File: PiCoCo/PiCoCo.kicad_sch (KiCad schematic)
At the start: 42 parts, among them P1 COCO-CART, Q2 2N7002, U1 Pico 2, U10 SN74LVC8T245DW, U11 SN74LVC245AD, U12 SN74LVC245AD, U13 SN74LVC245AD, U14 AMS1117-3.3, U15 SN74LVC1G11

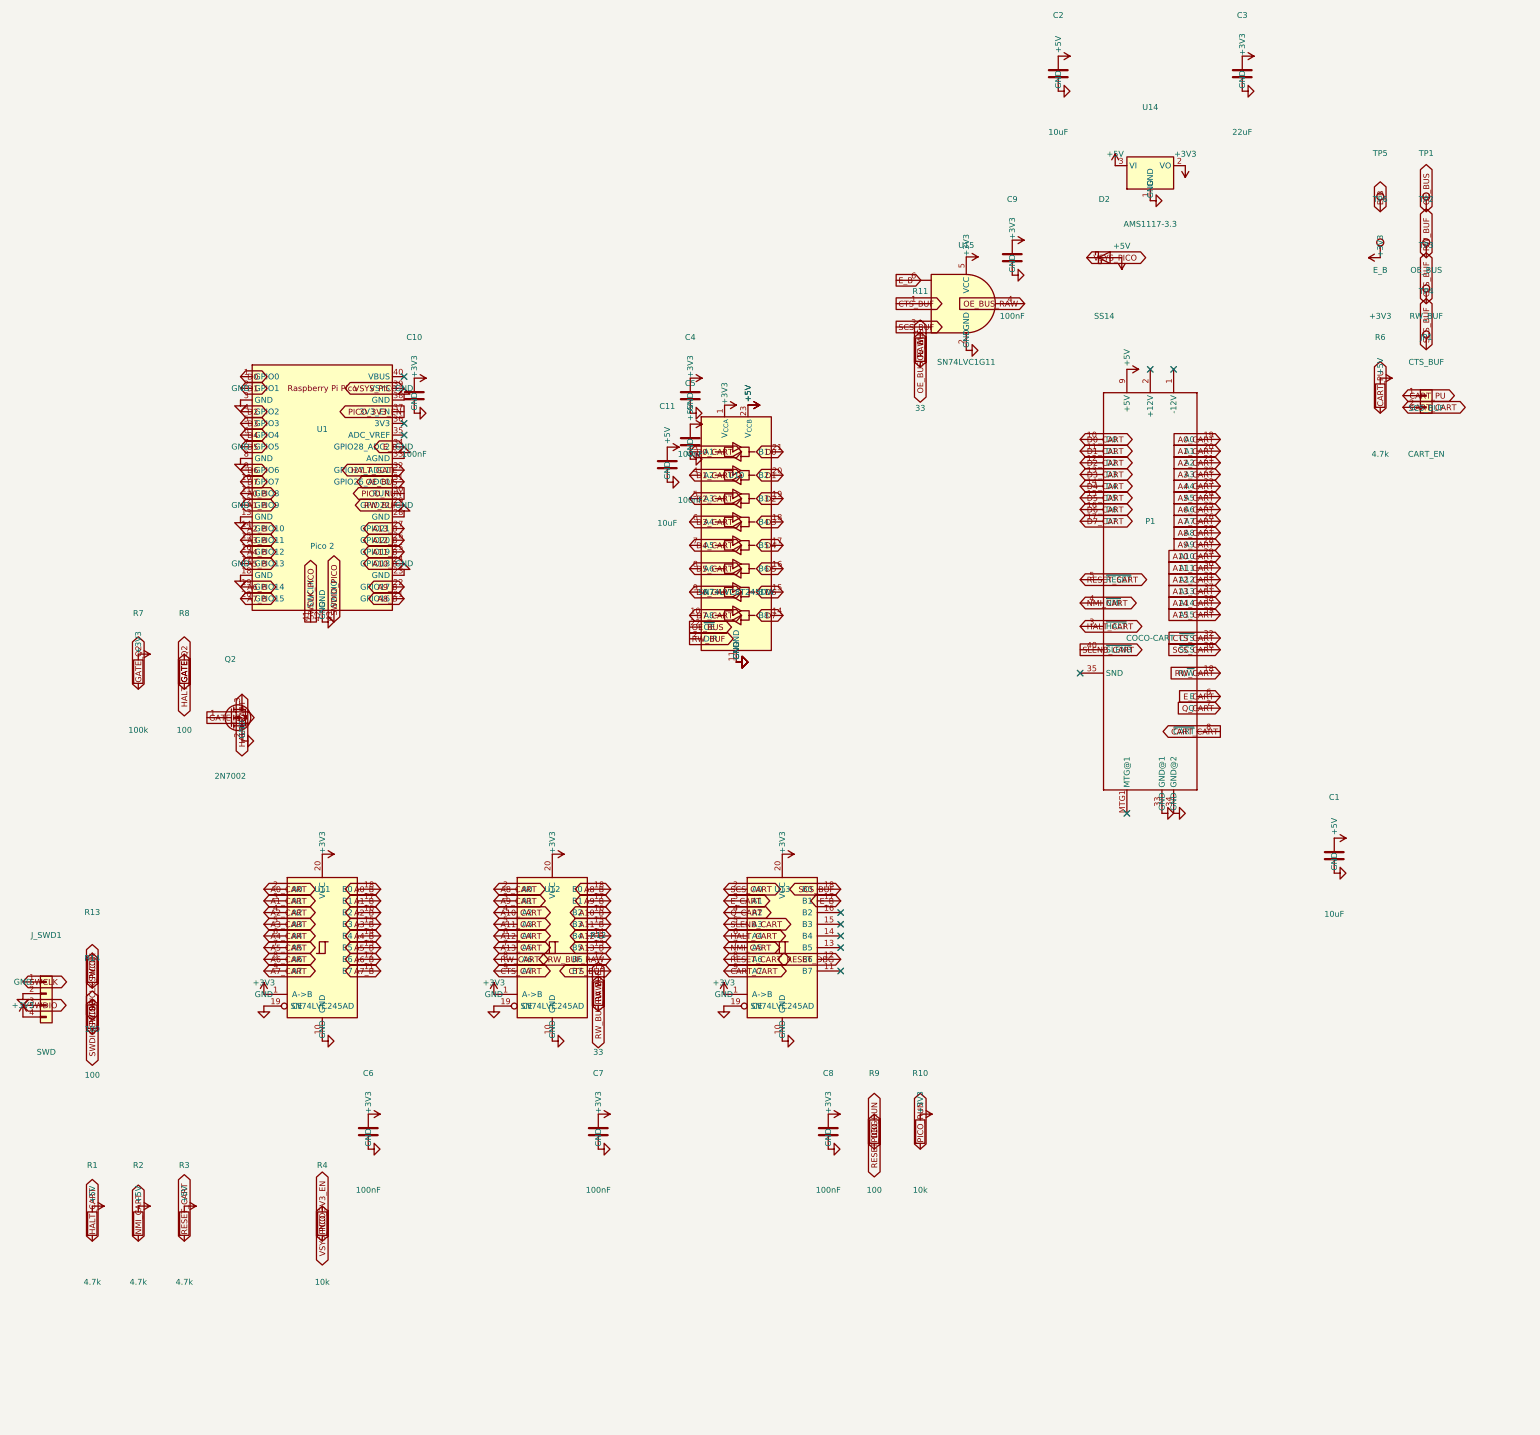
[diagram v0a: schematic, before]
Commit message: kicad: schematic v2.3 (LVC245 data buffer, 74LVC00 NAND-NAND decode, Plus-W pads, JP2/JP3, sound stage, LCSC properties, self-check)
Co-Authored-By: Claude Sonnet 5 <noreply@anthropic.com>
Claude-Session: https://claude.ai/code/session_013jbrP69zFzwzxjawTKy2c7
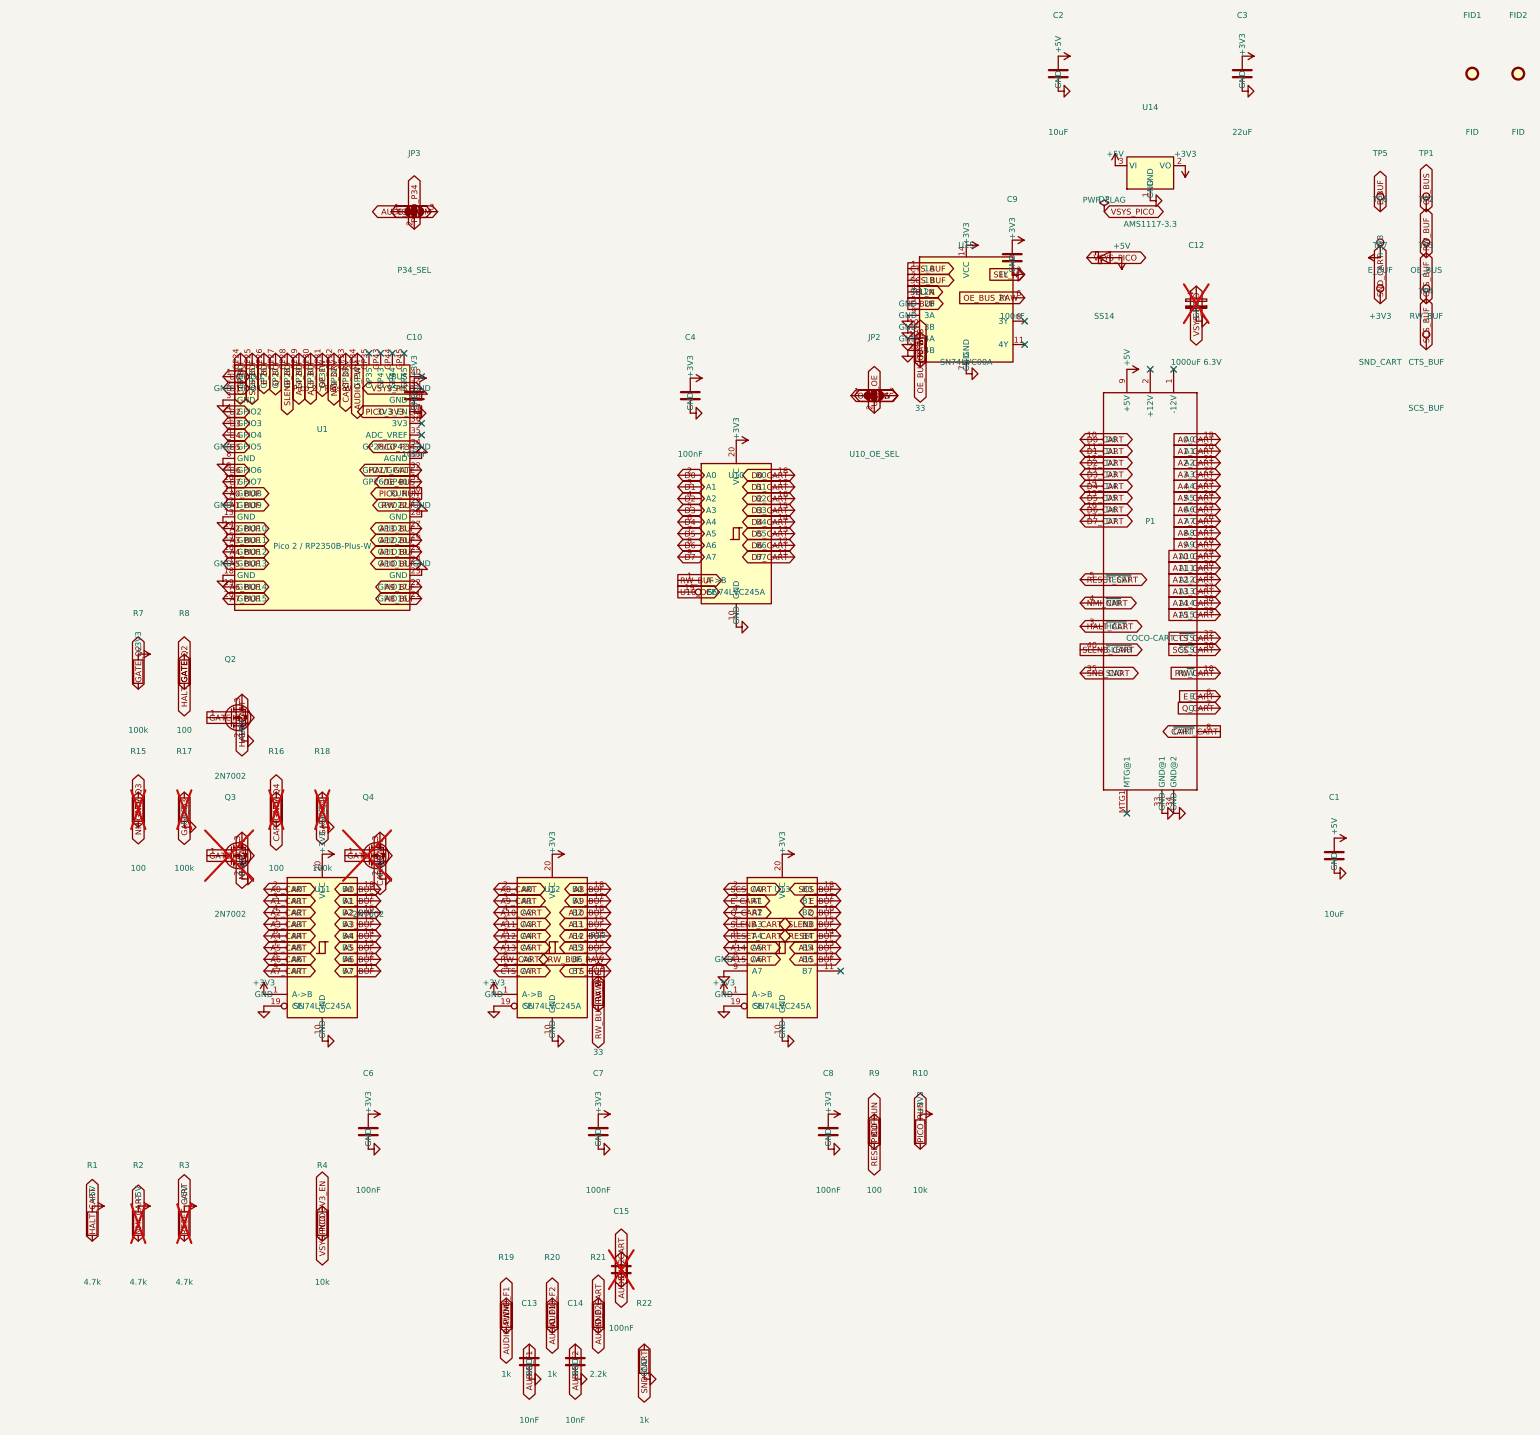
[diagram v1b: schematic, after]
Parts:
- removed C11: 10uF, Capacitor_SMD:C_0805_2012Metric, symbol Device:C
- removed C5: 100nF, Capacitor_SMD:C_0805_2012Metric, symbol Device:C
- removed JP1: CART_EN, Connector_PinHeader_2.54mm:PinHeader_1x02_P2.54mm_Vertical, symbol Connector_Generic:Conn_01x02
- removed J_SWD1: SWD, Connector_PinHeader_2.54mm:PinHeader_1x04_P2.54mm_Vertical, symbol Connector_Generic:Conn_01x04
- removed R13, R14: 100, Resistor_SMD:R_0805_2012Metric, symbol Device:R
- removed R6: 4.7k, Resistor_SMD:R_0805_2012Metric, symbol Device:R
- removed U1: Pico 2, PiCoCo:RPi_Pico_SMD_TH, symbol PiCoCo:Pico
- removed U10: SN74LVC8T245DW, Package_SO:SOIC-24W_7.5x15.4mm_P1.27mm, symbol Logic_LevelTranslator:SN74LVC8T245
- removed U15: SN74LVC1G11, Package_TO_SOT_SMD:SOT-363_SC-70-6, symbol 74xGxx:74LVC1G11
- added C12: 1000uF 6.3V, Capacitor_SMD:CP_Elec_8x10, symbol Device:C_Polarized
- added C13, C14: 10nF, Capacitor_SMD:C_0805_2012Metric, symbol Device:C
- added C15: 100nF, Capacitor_SMD:C_0805_2012Metric, symbol Device:C
- added FID1, FID2: FID, Fiducial:Fiducial_1mm_Mask2mm, symbol Mechanical:Fiducial
- added JP2: U10_OE_SEL, Jumper:SolderJumper-3_P1.3mm_Bridged12_RoundedPad1.0x1.5mm, symbol Jumper:SolderJumper_3_Bridged12
- added JP3: P34_SEL, Jumper:SolderJumper-3_P1.3mm_Bridged12_RoundedPad1.0x1.5mm, symbol Jumper:SolderJumper_3_Bridged12
- added Q3, Q4: 2N7002, Package_TO_SOT_SMD:SOT-23, symbol Transistor_FET:Q_NMOS_GSD
- added R15, R16: 100, Resistor_SMD:R_0805_2012Metric, symbol Device:R
- added R17, R18: 100k, Resistor_SMD:R_0805_2012Metric, symbol Device:R
- added R19, R20, R22: 1k, Resistor_SMD:R_0805_2012Metric, symbol Device:R
- added R21: 2.2k, Resistor_SMD:R_0805_2012Metric, symbol Device:R
- added TP7: SND_CART, TestPoint:TestPoint_Pad_1.0x1.0mm, symbol Connector:TestPoint
- added U1: Pico 2 / RP2350B-Plus-W, PiCoCo:Pico-Carrier, symbol PiCoCo:Pico-Carrier
- added U10: SN74LVC245A, Package_SO:SOIC-20W_7.5x12.8mm_P1.27mm, symbol 74xx:74LS245
- added U15: SN74LVC00A, Package_SO:SOIC-14_3.9x8.7mm_P1.27mm, symbol PiCoCo:74LVC00
- C1, C2: LCSC (none) -> C15850; MPN (none) -> 0805 10uF
- C10, C4, C6, C7, C8, C9: LCSC (none) -> C49678; MPN (none) -> 0805 100nF
- C3: LCSC (none) -> C45783; MPN (none) -> 0805 22uF
- D2: LCSC (none) -> C2480; MPN (none) -> SS14
- P1, TP1, TP2, TP3, TP4, TP6: now left out of the parts list
- Q2: LCSC (none) -> C8545; MPN (none) -> 2N7002
- R1: LCSC (none) -> C17673; MPN (none) -> 0805 4.7k 1%
- R10, R4: LCSC (none) -> C17414; MPN (none) -> 0805 10k 1%
- R11, R12: LCSC (none) -> C17634; MPN (none) -> 0805 33 1%
- R2, R3: LCSC (none) -> C17673; MPN (none) -> 0805 4.7k 1%; now not fitted
- R7: LCSC (none) -> C17407; MPN (none) -> 0805 100k 1%
- R8, R9: LCSC (none) -> C17408; MPN (none) -> 0805 100 1%
- TP5: value E_B -> E_BUF; now left out of the parts list
- U11, U12, U13: value SN74LVC245AD -> SN74LVC245A; LCSC (none) -> C571201; MPN (none) -> SN74LVC245ADWR
- U14: LCSC (none) -> C6186; MPN (none) -> AMS1117-3.3
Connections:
- net +3V3: now also U10.20 (VCC), U15.14 (VCC)
- net A14_CART: now also U13.7 (A5)
- net A15_CART: now also U13.8 (A6)
- net CART_CART: now also Q4.3 (D); no longer U13.9 (A7)
- net CTS_BUF: now also U1.GP24, U15.1 (1A)
- net D0: now also U1.1 (GPIO0), U10.2 (A0)
- net D0_CART: now also U10.18 (B0)
- net D1: now also U1.2 (GPIO1), U10.3 (A1)
- net D1_CART: now also U10.17 (B1)
- net D2: now also U1.4 (GPIO2), U10.4 (A2)
- net D2_CART: now also U10.16 (B2)
- net D3: now also U1.5 (GPIO3), U10.5 (A3)
- net D3_CART: now also U10.15 (B3)
- net D4: now also U1.6 (GPIO4), U10.6 (A4)
- net D4_CART: now also U10.14 (B4)
- net D5: now also U1.7 (GPIO5), U10.7 (A5)
- net D5_CART: now also U10.13 (B5)
- net D6: now also U1.9 (GPIO6), U10.8 (A6)
- net D6_CART: now also U10.12 (B6)
- net D7: now also U1.10 (GPIO7), U10.9 (A7)
- net D7_CART: now also U10.11 (B7)
- net GND: now also U13.9 (A7), C12.2, C13.2, C14.2, Q3.2 (S), Q4.2 (S), R17.2, R18.2, R22.2, U1.13 (GND), U1.18 (GND), U1.23 (GND), U1.28 (GND), U1.3 (GND), U1.33 (AGND), U1.38 (GND), U1.8 (GND), U10.10 (GND), U15.10 (3B), U15.12 (4A), U15.13 (4B), U15.7 (GND), U15.9 (3A)
- net HALT_CART: no longer U13.6 (A4)
- net HALT_GATE: now also U1.32 (GP27/GP41)
- net NMI_CART: now also Q3.3 (D); no longer U13.7 (A5)
- net OE_BUS: now also JP2.1 (A), U1.31 (GP26/GP40)
- net OE_BUS_RAW: now also U15.6 (2Y)
- net PICO_3V3_EN: now also U1.37 (3V3_EN)
- net PICO_RUN: now also U1.30 (RUN)
- net RESET_CART: now also U13.6 (A4); no longer U13.8 (A6)
- net RW_BUF: now also U1.29 (GPIO22), U10.1 (A->B)
- net SCS_BUF: now also U1.GP25, U15.2 (1B)
- net VSYS_PICO: now also C12.1, U1.39 (VSYS)
- net SND_CART: now reaches P1.35 (SND)
- net SND_CART: now also C15.2, R21.2, R22.1, TP7.1
- net A14_BUF: now reaches U13.13 (B5)
- net A14_BUF: now also U1.GP29
- net RESET_BUF: now reaches U13.14 (B4)
- net RESET_BUF: now also R9.1
- net SLENB_BUF: now reaches U13.15 (B3)
- net SLENB_BUF: now also U1.GP28
- net Q_BUF: now reaches U13.16 (B2)
- net Q_BUF: now also U1.GP27
- net A0_B renamed A0_BUF
- net A0_BUF: now also U1.11 (GPIO8)
- net A10_B renamed A10_BUF
- net A10_BUF: now also U1.24 (GPIO18)
- net A11_B renamed A11_BUF
- net A11_BUF: now also U1.25 (GPIO19)
- net A12_B renamed A12_BUF
- net A12_BUF: now also U1.26 (GPIO20)
- net A13_B renamed A13_BUF
- net A13_BUF: now also U1.27 (GPIO21)
- net A1_B renamed A1_BUF
- net A1_BUF: now also U1.12 (GPIO9)
- net A2_B renamed A2_BUF
- net A2_BUF: now also U1.14 (GPIO10)
- net A3_B renamed A3_BUF
- net A3_BUF: now also U1.15 (GPIO11)
- net A4_B renamed A4_BUF
- net A4_BUF: now also U1.16 (GPIO12)
- net A5_B renamed A5_BUF
- net A5_BUF: now also U1.17 (GPIO13)
- net A6_B renamed A6_BUF
- net A6_BUF: now also U1.19 (GPIO14)
- net A7_B renamed A7_BUF
- net A7_BUF: now also U1.20 (GPIO15)
- net A8_B renamed A8_BUF
- net A8_BUF: now also U1.21 (GPIO16)
- net A9_B renamed A9_BUF
- net A9_BUF: now also U1.22 (GPIO17)
- net E_B renamed E_BUF
- net E_BUF: now also JP3.1 (A), U1.GP26, U15.5 (2B)
- net RESET_DBG renamed A15_BUF
- net A15_BUF: now also U1.GP30; no longer R9.1
- new net AUDIO_F1: C13.1, R19.2, R20.1
- new net AUDIO_F2: C14.1, C15.1, R20.2, R21.1
- new net AUDIO_PWM: JP3.3 (B), R19.1, U1.GP34
- new net CART_DRV: R16.1, U1.GP33
- new net GATE_Q3: Q3.1 (G), R15.2, R17.1
- new net GATE_Q4: Q4.1 (G), R16.2, R18.1
- new net NMI_DRV: R15.1, U1.GP32
- new net OE_FW: JP2.3 (B), U1.GP31
- new net PICO_P34: JP3.2 (C), U1.34 (GP28/GP42)
- new net SEL_N: U15.3 (1Y), U15.4 (2A)
- new net U10_OE: JP2.2 (C), U10.19 (CE)
- no-connect marks 12 -> 13

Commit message: kicad: place_pcb rotates pad/text angles with the footprint; drop MTG1; strip debug silk; board text fixes
F1: place_pcb.py's PLACEMENT-driven rotation only updated a footprint's own
(at X Y rot); KiCad stores every pad/fp_text/property (at x y [angle]) as an
ABSOLUTE angle, so pad copper/text shapes went stale relative to the newly
rotated footprint (the 76 U1-only shorting_items and every rotated 0805's
DRC noise). Added _rotate_child_angles() (adds the rotation delta to every
child's angle, inserting one where absent; positions are untouched, they're
footprint-local and KiCad reinterprets them under the new rotation itself)
and an assert-based self-check that every pad's absolute angle matches its
footprint's rotation. Verified via unit tests, against a scratch copy of the
current board (delta=0 no-op confirmed, a fabricated delta=90 confirmed
correct), and against the pre-sync board from 3dce2a9 (delta math verified
correct on the old U1 footprint despite its self-check-incompatible mixed
per-pad library angles).

F2: P1's MTG1 mounting-hole pad (11mm pad/8mm drill) sits inside the v2.3
module's body corner regardless of rotation -- removed via new
fix_cart_footprint() (renamed from trim_cart_fingers()) and fix_cart_symbol()
in gen_schematic.py, with check_library.py assertions and idempotency
verified.

F3: Pico-Carrier's SWDIO/SWCLK silkscreen labels (debug pads 41-43 were
already removed) stripped in write_carrier_footprint(); check_library.py's
F.SilkS count guard and assertions updated.

F4: add_board_extras() now deletes the stale v0.1 gr_text banner left under
the module, mirrors any B.-layer text (JLCJLCJLCJLC), and raises the JP2/JP3
legend text size from 0.6mm (below the board's DRC minimum) to 0.8mm.

Regenerated PiCoCo.kicad_sch; check_library.py and ERC (1 error, the known
GND@1/GND@2 quirk; 0 warnings) both clean. PiCoCo.kicad_pcb intentionally
NOT touched this round -- the controller will restore it to pre-sync state
and redo the GUI sync before r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
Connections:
- no-connect marks 13 -> 12
